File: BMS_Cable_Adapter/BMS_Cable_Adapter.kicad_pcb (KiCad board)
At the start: 2 copper layers, 115 x 105 mm, 3 parts, among them J1 MicroFit_18Pin, J2 MicroFit_10Pin, J3 32Pin JAE

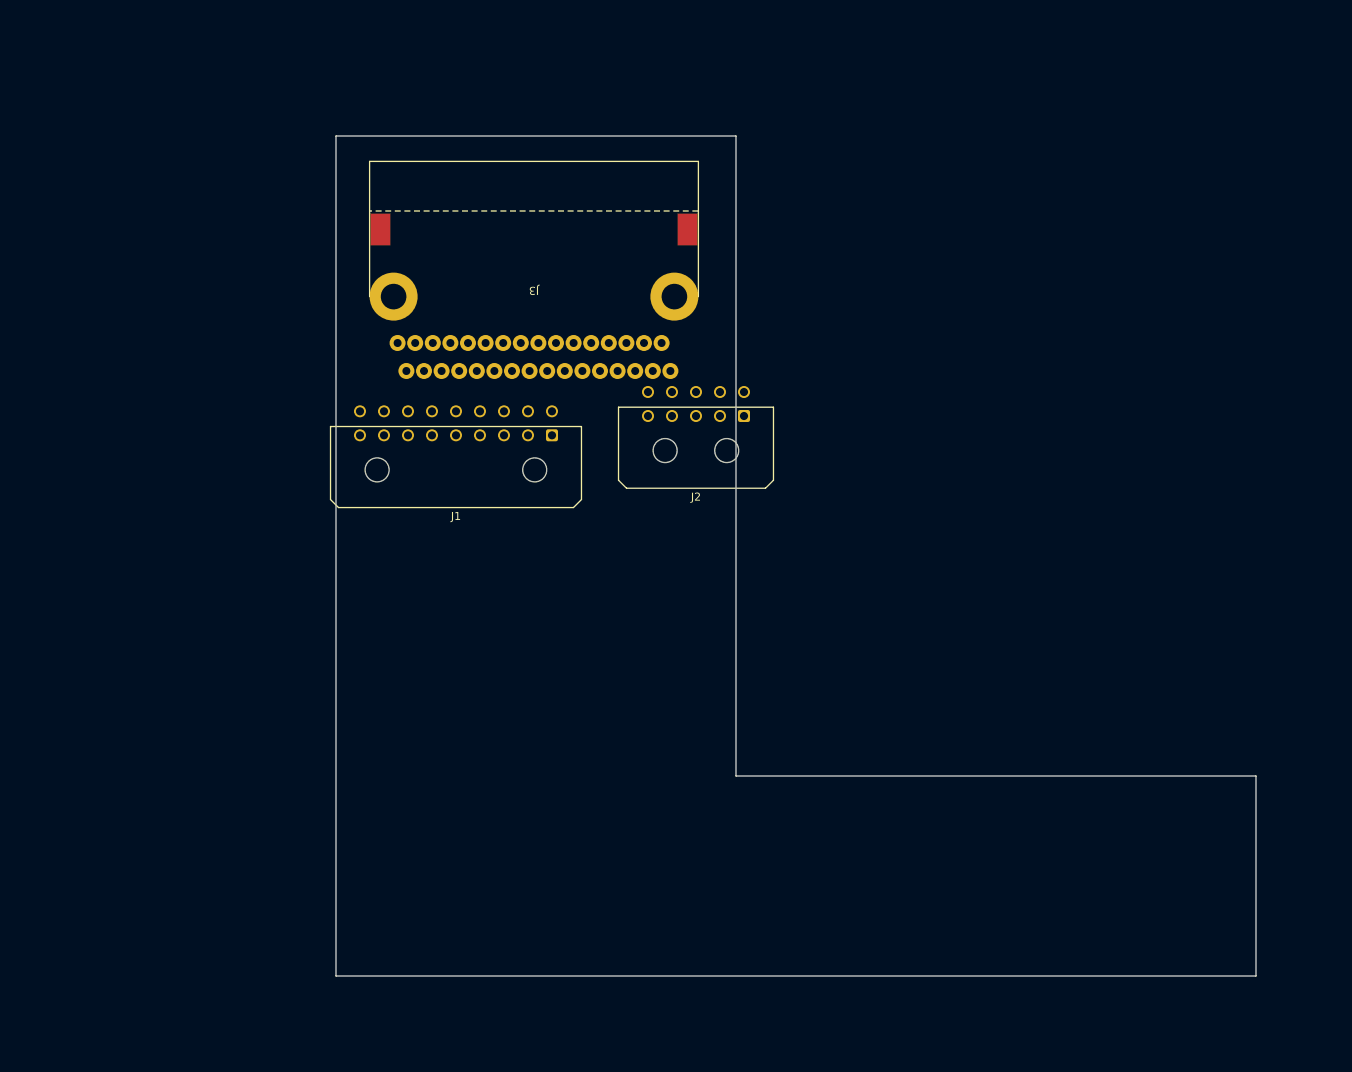
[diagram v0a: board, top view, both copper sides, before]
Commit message: BMS Cable adapter done
Also libraries updated
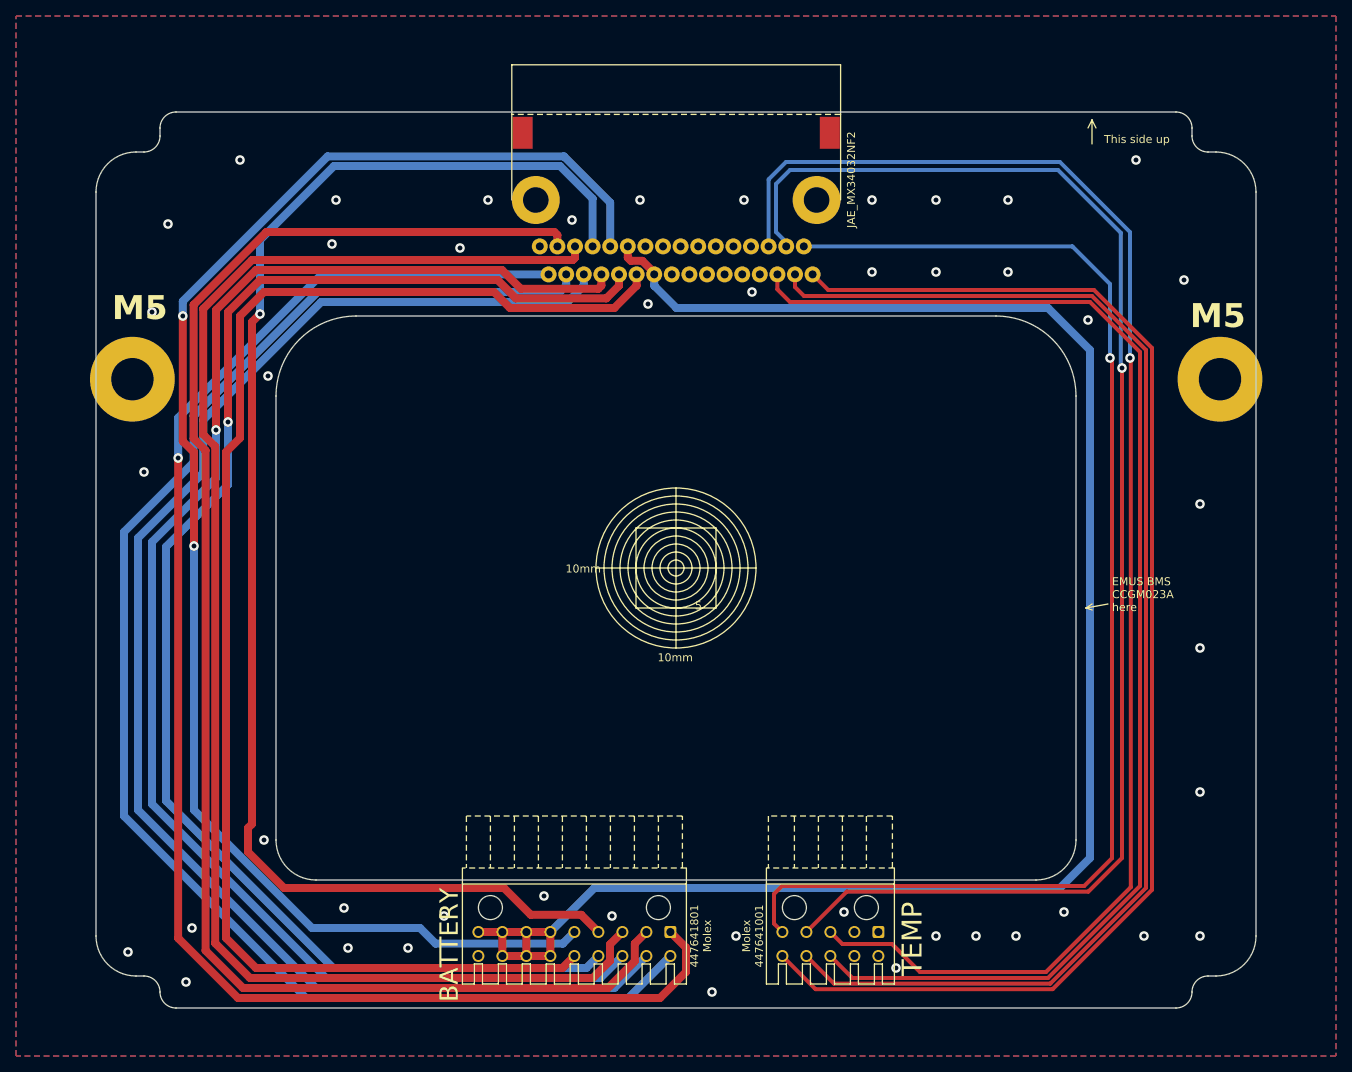
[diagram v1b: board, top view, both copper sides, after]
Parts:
- added H1: MountingHole M5, MountingHole:MountingHole_5.3mm_M5_Pad, F.Cu at (69.5, 70.4)
- added H2: MountingHole M5, MountingHole:MountingHole_5.3mm_M5_Pad, F.Cu at (205.5, 70.4)
- added SYM1: Logo_Open_Hardware_Small, Calibration_Scale:Gauge_10mm_Type3_SilkScreenTop, F.Cu at (137.5, 94.0)
- J1: value MicroFit_18Pin -> MicroFit_18Pin_Receptacle_Header; footprint Connector_Molex:Molex_Micro-Fit_3.0_43045-1800_2x09_P3.00mm_Horizontal -> 0_user_lib:Molex_Micro-Fit_BMI_Receptacle_18Pin_44764
- J2: value MicroFit_10Pin -> MicroFit_10Pin_Receptacle_Header; footprint Connector_Molex:Molex_Micro-Fit_3.0_43045-1000_2x05_P3.00mm_Horizontal -> 0_user_lib:Molex_Micro-Fit_BMI_Receptacle_10Pin_44764
- moved J2 65.4 mm to (156.8, 139.5)
- moved J1 62.1 mm to (124.8, 139.5)
- moved J3 21.5 mm to (137.5, 48.0)
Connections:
- J1 pad 1: unconnected-(J1-Pin_1-Pad1) -> /(-)
- J1 pad 10: unconnected-(J1-Pin_10-Pad10) -> /1+
- J1 pad 11: unconnected-(J1-Pin_11-Pad11) -> /3+
- J1 pad 12: unconnected-(J1-Pin_12-Pad12) -> /5+
- J1 pad 13: unconnected-(J1-Pin_13-Pad13) -> /7+
- J1 pad 14: unconnected-(J1-Pin_14-Pad14) -> /9+
- J1 pad 15: unconnected-(J1-Pin_15-Pad15) -> /10+
- J1 pad 16: unconnected-(J1-Pin_16-Pad16) -> /10+
- J1 pad 17: unconnected-(J1-Pin_17-Pad17) -> /10+
- J1 pad 2: unconnected-(J1-Pin_2-Pad2) -> /2+
- J1 pad 3: unconnected-(J1-Pin_3-Pad3) -> /4+
- J1 pad 4: unconnected-(J1-Pin_4-Pad4) -> /6+
- J1 pad 5: unconnected-(J1-Pin_5-Pad5) -> /8+
- J1 pad 6: unconnected-(J1-Pin_6-Pad6) -> /10+
- J1 pad 7: unconnected-(J1-Pin_7-Pad7) -> /10+
- J1 pad 8: unconnected-(J1-Pin_8-Pad8) -> /10+
- J1 pad 9: unconnected-(J1-Pin_9-Pad9) -> /10+
- J2 pad 10: unconnected-(J2-Pin_10-Pad10) -> /T1+
- J2 pad 3: unconnected-(J2-Pin_3-Pad3) -> /T3-
- J2 pad 4: unconnected-(J2-Pin_4-Pad4) -> /T2-
- J2 pad 5: unconnected-(J2-Pin_5-Pad5) -> /T1-
- J2 pad 8: unconnected-(J2-Pin_8-Pad8) -> /T3+
- J2 pad 9: unconnected-(J2-Pin_9-Pad9) -> /T2+
- J3 pad 1: unconnected-(J3-Pin_1-Pad1) -> /(-)
- J3 pad 14: unconnected-(J3-Pin_14-Pad14) -> /T3+
- J3 pad 15: unconnected-(J3-Pin_15-Pad15) -> /T2+
- J3 pad 16: unconnected-(J3-Pin_16-Pad16) -> /T1+
- J3 pad 18: unconnected-(J3-Pin_18-Pad18) -> /2+
- J3 pad 19: unconnected-(J3-Pin_19-Pad19) -> /4+
- J3 pad 2: unconnected-(J3-Pin_2-Pad2) -> /1+
- J3 pad 20: unconnected-(J3-Pin_20-Pad20) -> /6+
- J3 pad 21: unconnected-(J3-Pin_21-Pad21) -> /8+
- J3 pad 22: unconnected-(J3-Pin_22-Pad22) -> /10+
- J3 pad 3: unconnected-(J3-Pin_3-Pad3) -> /3+
- J3 pad 30: unconnected-(J3-Pin_30-Pad30) -> /T3-
- J3 pad 31: unconnected-(J3-Pin_31-Pad31) -> /T2-
- J3 pad 32: unconnected-(J3-Pin_32-Pad32) -> /T1-
- J3 pad 4: unconnected-(J3-Pin_4-Pad4) -> /5+
- J3 pad 5: unconnected-(J3-Pin_5-Pad5) -> /7+
- J3 pad 6: unconnected-(J3-Pin_6-Pad6) -> /9+
- J3 pad 7: unconnected-(J3-Pin_7-Pad7) -> /10+
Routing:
- net /10+: track 0.00 -> 223.9 mm
- net /2+: track 0.00 -> 193.4 mm
- net /(-): track 0.00 -> 192.5 mm, vias 0 -> 1
- net /1+: track 0.00 -> 188.2 mm
- net /8+: track 0.00 -> 188.0 mm, vias 0 -> 2
- net /5+: track 0.00 -> 186.8 mm, vias 0 -> 1
- net /4+: track 0.00 -> 186.7 mm
- net /T3-: track 0.00 -> 184.0 mm, vias 0 -> 1
- net /3+: track 0.00 -> 182.5 mm
- net /7+: track 0.00 -> 181.2 mm, vias 0 -> 1
- net /9+: track 0.00 -> 178.4 mm
- net /6+: track 0.00 -> 178.1 mm, vias 0 -> 1
- net /T2-: track 0.00 -> 176.9 mm, vias 0 -> 1
- net /T1+: track 0.00 -> 167.0 mm
- net /T2+: track 0.00 -> 164.8 mm
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- added copper zone on B.Cu, net GND
- added copper zone on F.Cu, net GND
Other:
- board size 115 x 105 mm -> 145 x 112 mm
- board text added: "447641801 Molex"
- board text added: "BATTERY"
- board text added: "BMS to Cell Adapter D. Vaitiekus AUGA Tech 2024-06-13 Rev. A"
- board text added: "EMUS BMS CCGM023A here"
- board text added: "JAE_MX34032NF2"
- board text added: "JLCJLCJLC"
- board text added: "M5"
- board text added: "Molex 447641001"
- board text added: "TEMP"
- board text added: "This side up"
